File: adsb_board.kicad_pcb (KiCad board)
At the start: 2 copper layers, 50 x 25 mm, 13 parts, among them J1 Conn_Coaxial, J2 Conn_Coaxial, J3 USB_B_Micro, U1 TA1090EC, U2 TA1090EC, U3 PSA4-5043+

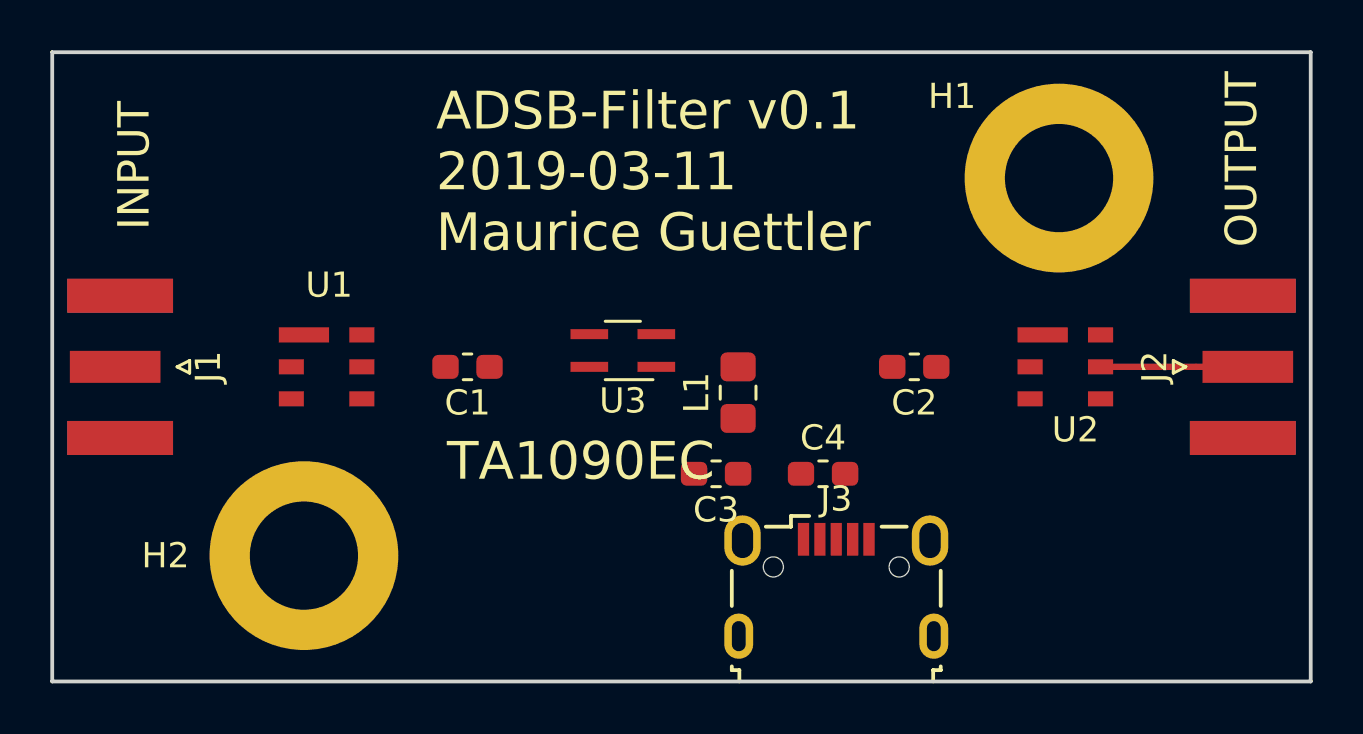
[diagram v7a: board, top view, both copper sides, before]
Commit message: update scheamtic
add vias along the signal trace in the layout
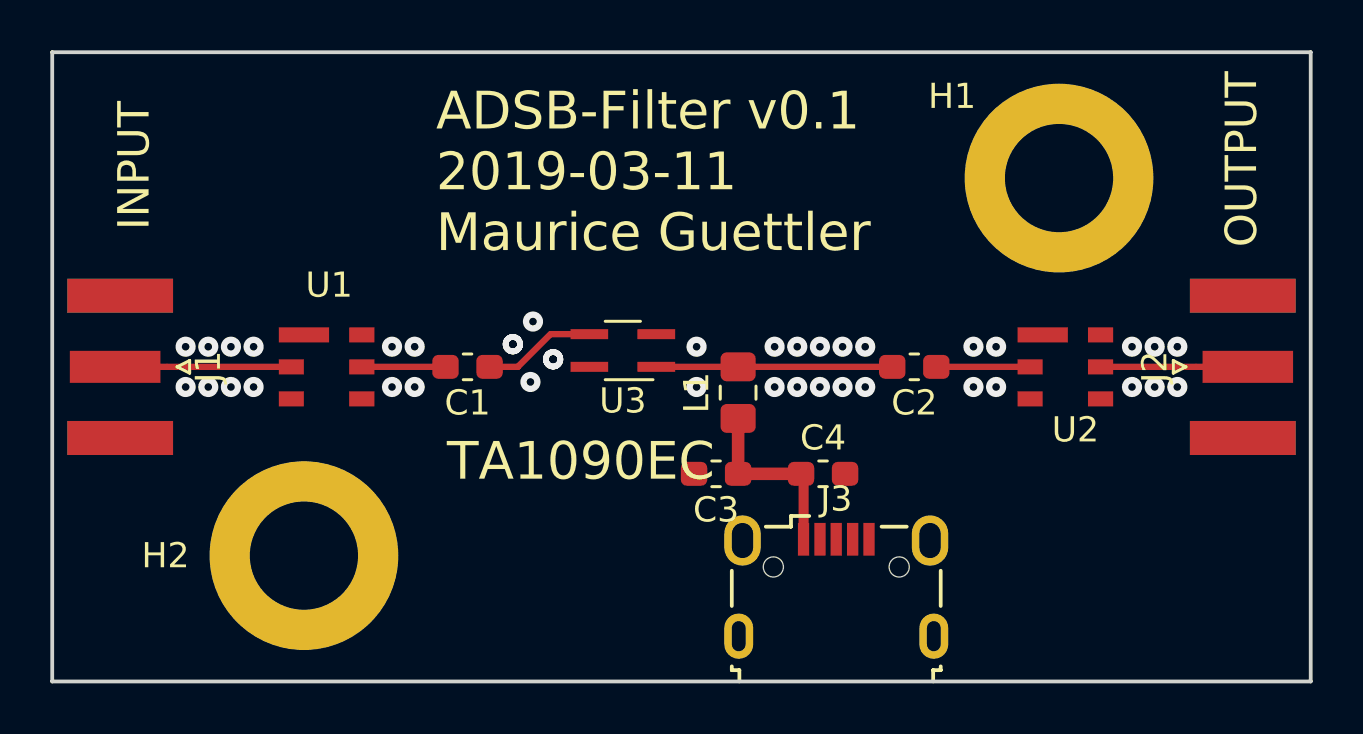
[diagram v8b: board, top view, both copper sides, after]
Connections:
- C3 pad 1: Net-(C3-Pad1) -> /VCC
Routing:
- net Net-(C2-Pad2): track 0.00 -> 9.38 mm
- net /VCC: track 0.00 -> 7.34 mm
- net /INPUT: track 0.00 -> 7.00 mm
- net Net-(C1-Pad1): track 0.00 -> 4.50 mm
- net Net-(C2-Pad1): track 0.00 -> 3.72 mm
- net Net-(C1-Pad2): track 0.00 -> 3.33 mm
- net /GND: vias 0 -> 42
- added copper zone on F.Cu, net /GND
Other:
- rule via_min_size: 0.4 -> 0.3
